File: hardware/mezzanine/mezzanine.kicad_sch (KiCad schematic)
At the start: 5 parts

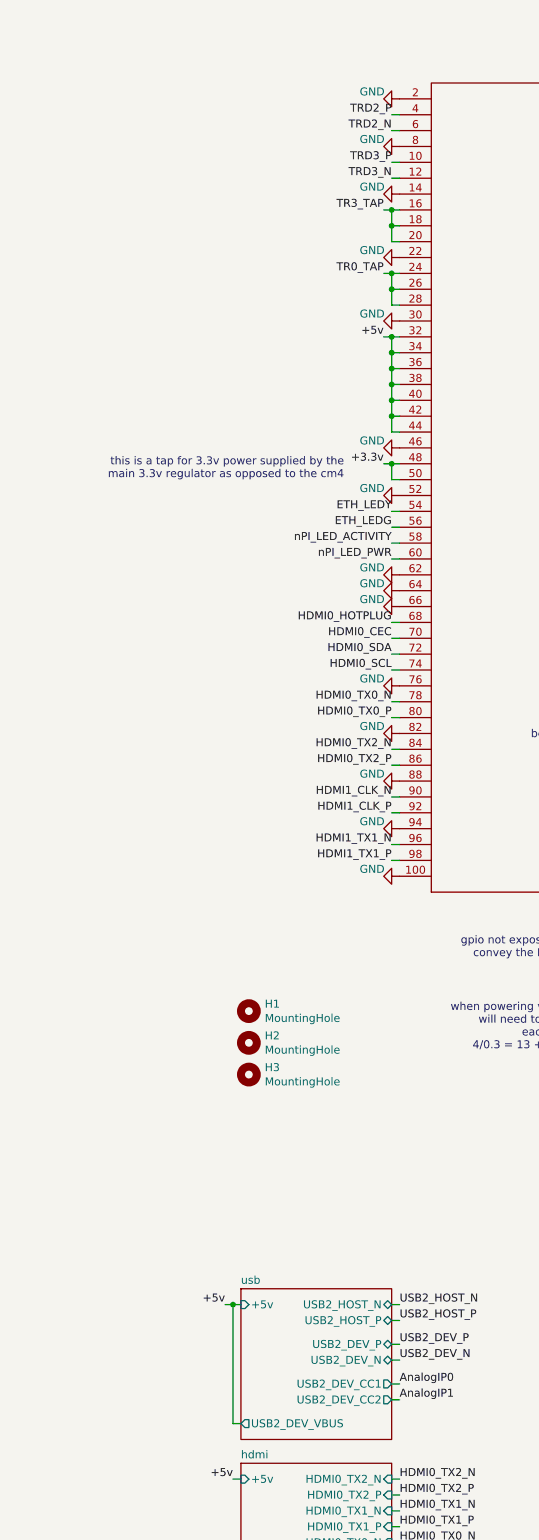
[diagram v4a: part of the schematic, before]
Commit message: tweak mezzanine
almost ready to order
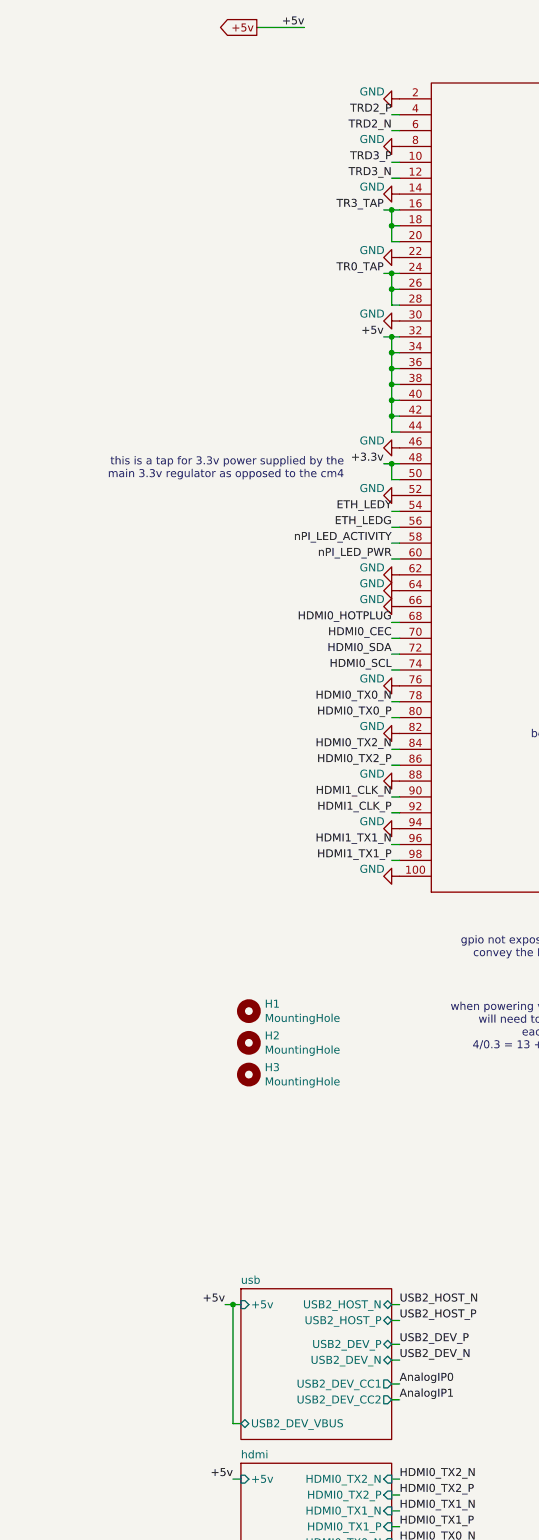
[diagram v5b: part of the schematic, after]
